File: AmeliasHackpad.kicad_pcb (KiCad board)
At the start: 2 copper layers, 62 x 40.9 mm, 7 parts, among them SW1 SW_Push, SW2 SW_Push, SW3 SW_Push, SW4 SW_Push

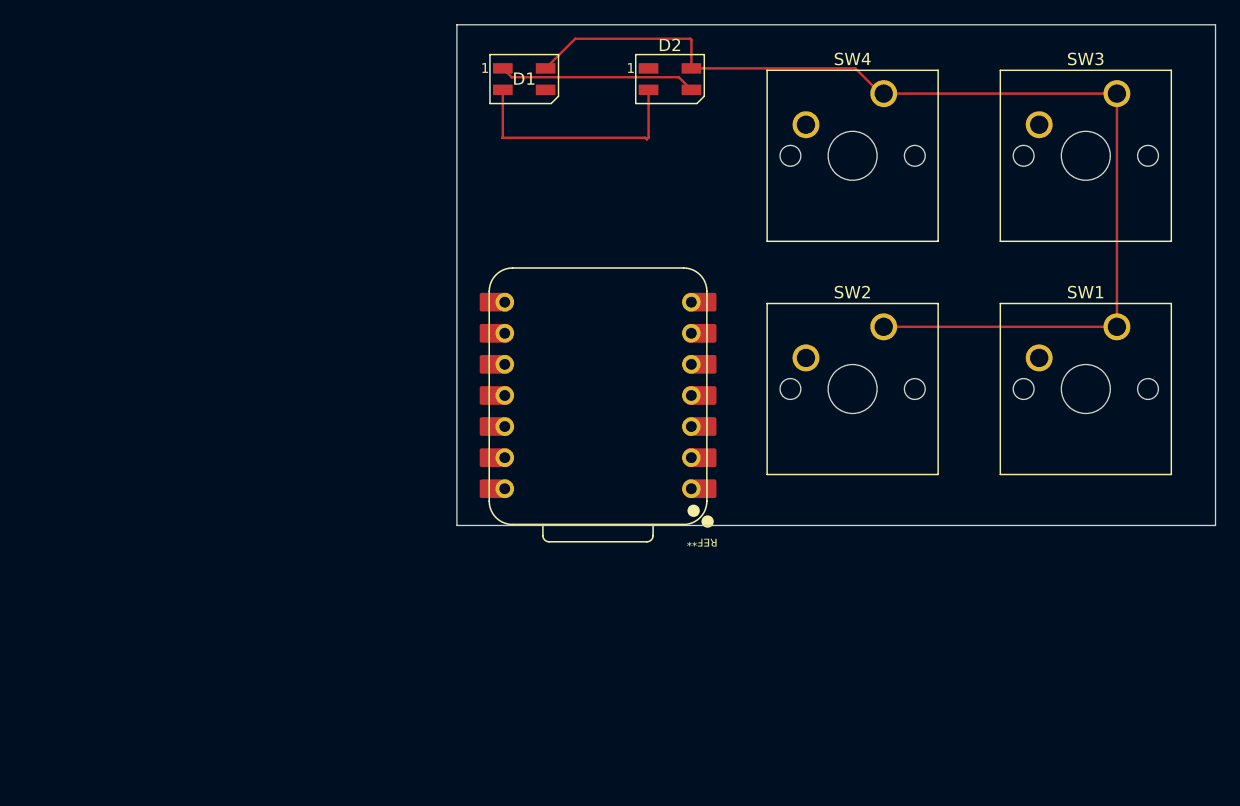
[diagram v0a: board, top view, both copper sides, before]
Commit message: Rotated PCB
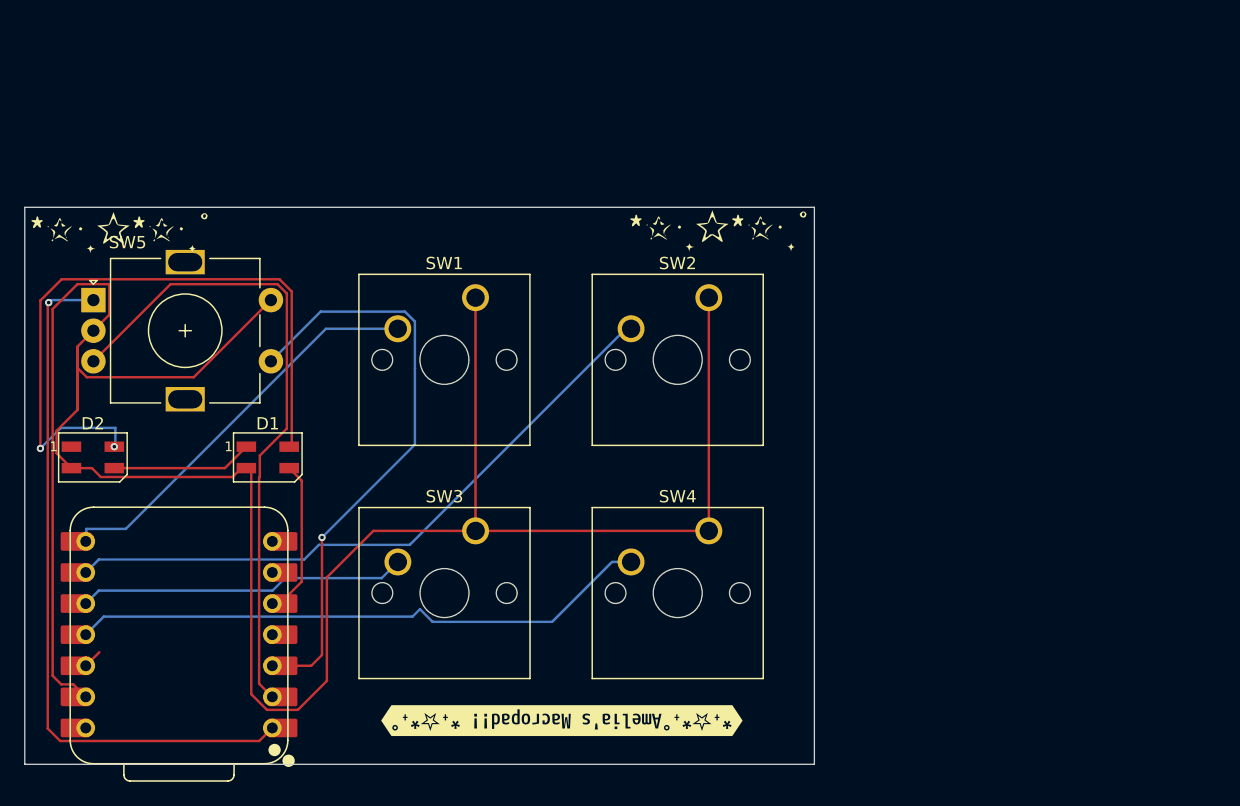
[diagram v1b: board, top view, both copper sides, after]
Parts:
- removed REF**: XIAO-RP2040-DIP, OPL_Library:XIAO-RP2040-DIP
- added G***: LOGO, LOGO, F.Cu at (140.5, 67.8)
- added G***: LOGO, LOGO, F.Cu at (189.4, 67.7)
- added G***: LOGO, LOGO, B.Cu at (187.6, 109.0)
- added SW5: RotaryEncoder_Switch, Rotary_Encoder:RotaryEncoder_Alps_EC11E-Switch_Vertical_H20mm, F.Cu at (138.0, 73.7)
- added U1: XIAO-RP2040-DIP, OPL:XIAO-RP2040-DIP, F.Cu at (145.0, 101.0)
- added kibuzzard-693A5F78: G***, kibuzzard-693A5F78, F.Cu at (176.3, 108.0)
- moved SW3 63.4 mm to (169.2, 92.6)
- moved D2 56.4 mm to (138.0, 86.5)
- moved SW1 52.4 mm to (169.2, 73.5)
- moved SW4 38.5 mm to (188.3, 92.6)
- moved D1 37.3 mm to (152.2, 86.5)
- moved SW2 14.5 mm to (188.3, 73.5)
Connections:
- D1 pad 2: +5V -> GND
- D1 pad 4: GND -> 5V
- D2 pad 2: +5V -> GND
- D2 pad 4: GND -> 5V
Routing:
- net GND: track 89.0 -> 201.1 mm
- net Net-(U1-GPIO26/ADC0/A0): track 0.00 -> 57.8 mm, vias 0 -> 1
- net 5V: track 0.00 -> 54.9 mm, vias 0 -> 2
- net Net-(U1-GPIO27/ADC1/A1): track 0.00 -> 53.1 mm
- net Net-(U1-GPIO2/SCK): track 0.00 -> 52.9 mm
- net Net-(U1-GPIO3/MOSI): track 0.00 -> 48.8 mm
- net Net-(U1-GPIO28/ADC2/A2): track 0.00 -> 48.6 mm, vias 0 -> 1
- net Net-(U1-GPIO1/RX): track 0.00 -> 34.1 mm
- net Net-(U1-GPIO4/MISO): track 0.00 -> 27.0 mm
- net +5V: track 19.9 -> 0.00 mm
- net Net-(D1-DIN): track 0.00 -> 12.8 mm
- net Net-(D1-DOUT): track 16.1 -> 11.5 mm
- net unconnected-(U1-3V3-Pad12): track 0.00 -> 1.57 mm
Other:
- board size 62 x 40.9 mm -> 64.5 x 45.5 mm
- board text added: "HI!"
